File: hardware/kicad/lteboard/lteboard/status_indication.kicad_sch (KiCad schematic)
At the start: 17 parts, among them U2 PCA9535PW

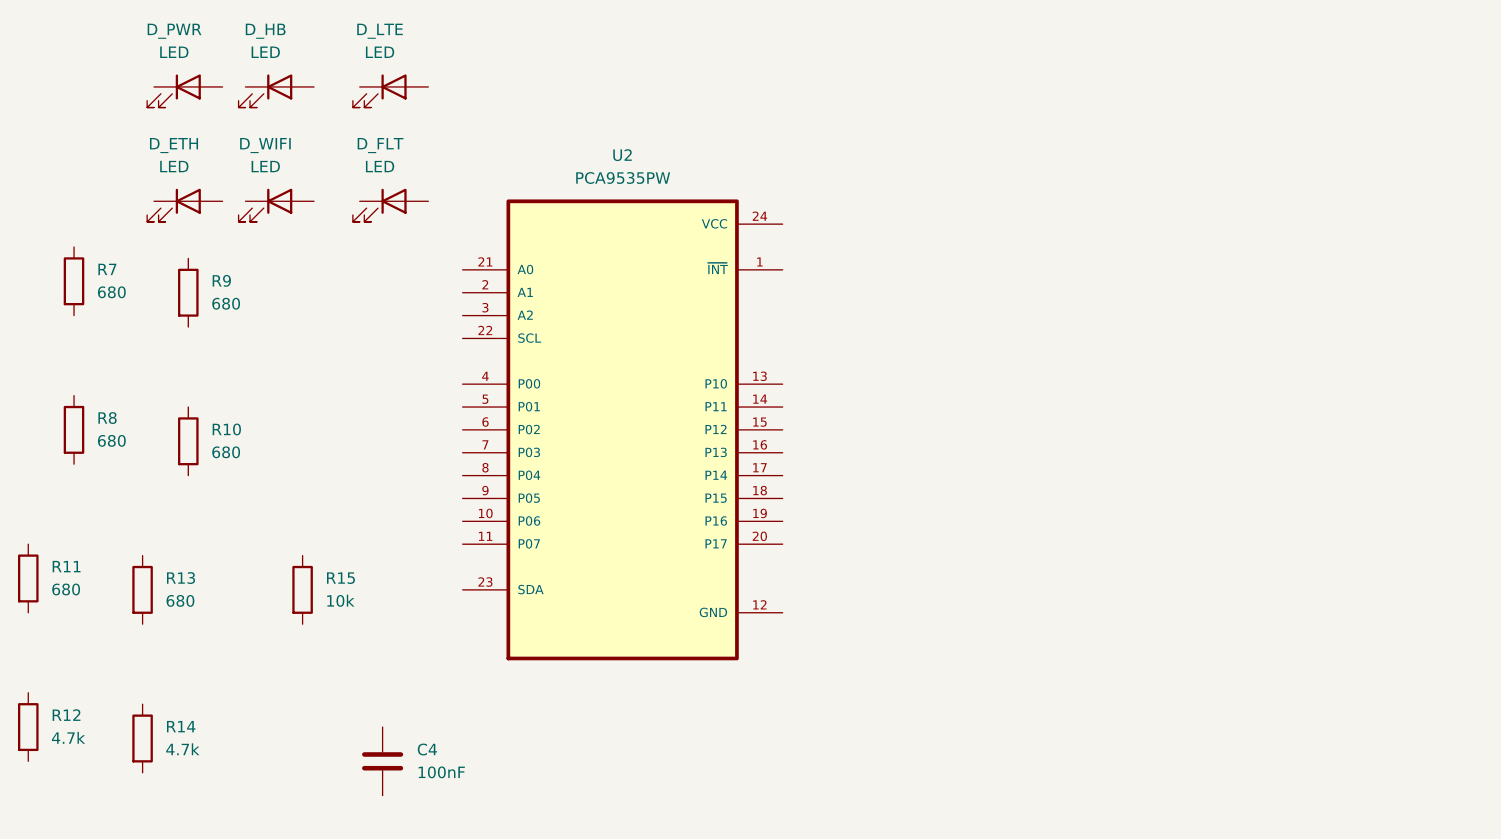
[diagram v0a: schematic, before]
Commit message: status-indication: complete schematic capture, cross-sheet wiring, docs, and BOM
- status_indication.kicad_sch: full wiring completed (address straps, power/ground,
  I2C pull-ups, INT pull-up, decoupling, 6 LED channels). Caught and fixed two real bugs
  via full programmatic connectivity verification (every pin/net reconstructed from the
  actual file, not just visual inspection): all 6 LEDs were initially wired with reversed
  polarity (would never have lit), and a new hierarchical 3V3_LOGIC label was placed
  floating (same name, no wire, so not actually part of the net). 10 spare GPIOs marked
  with No-Connect flags.
- core-compute.kicad_sch: converted 5 local GND_LOGIC labels to global_label (same class
  of bug fixed in power.kicad_sch during analog-io's ERC pass -- would have left this new
  sheet's ground isolated from the MCU's). Added I2C_SDA/I2C_SCL (Bidirectional, on
  GPIO8/GPIO9) and 3V3_LOGIC (Passive) hierarchical labels for cross-sheet export.
  Confirmed J1's 4 VBUS pins share one schematic pin location by symbol design, so the
  existing single No-Connect flag already covers all 4 -- no gap there.
- lteboard.kicad_sch: wired the two sheet symbols together (I2C_SDA, I2C_SCL, 3V3_LOGIC),
  verified pin types match on both ends (Passive/Passive, Bidirectional/Bidirectional x2)
  and wire endpoints land exactly on the corresponding pins.
- Added docs/subsystems/status-indication.md (full build-plan writeup, Steps 1-8) and
  hardware/bom/status_indication_bom.csv (10 parts).
- docs/roadmap.md: item 5 (status indication) marked DONE; backfilled item 4 (relay
  outputs) to DONE too, since it was already complete but never marked here.
- docs/build-log.md: added the status-indication entry, and backfilled the relay-outputs
  entry that was missing.

ERC deferred to a single project-wide pass once every subsystem is built, per current
project decision (not run per-subsystem here, unlike analog-io).

Deliberately not included: uncommitted analog-io changes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
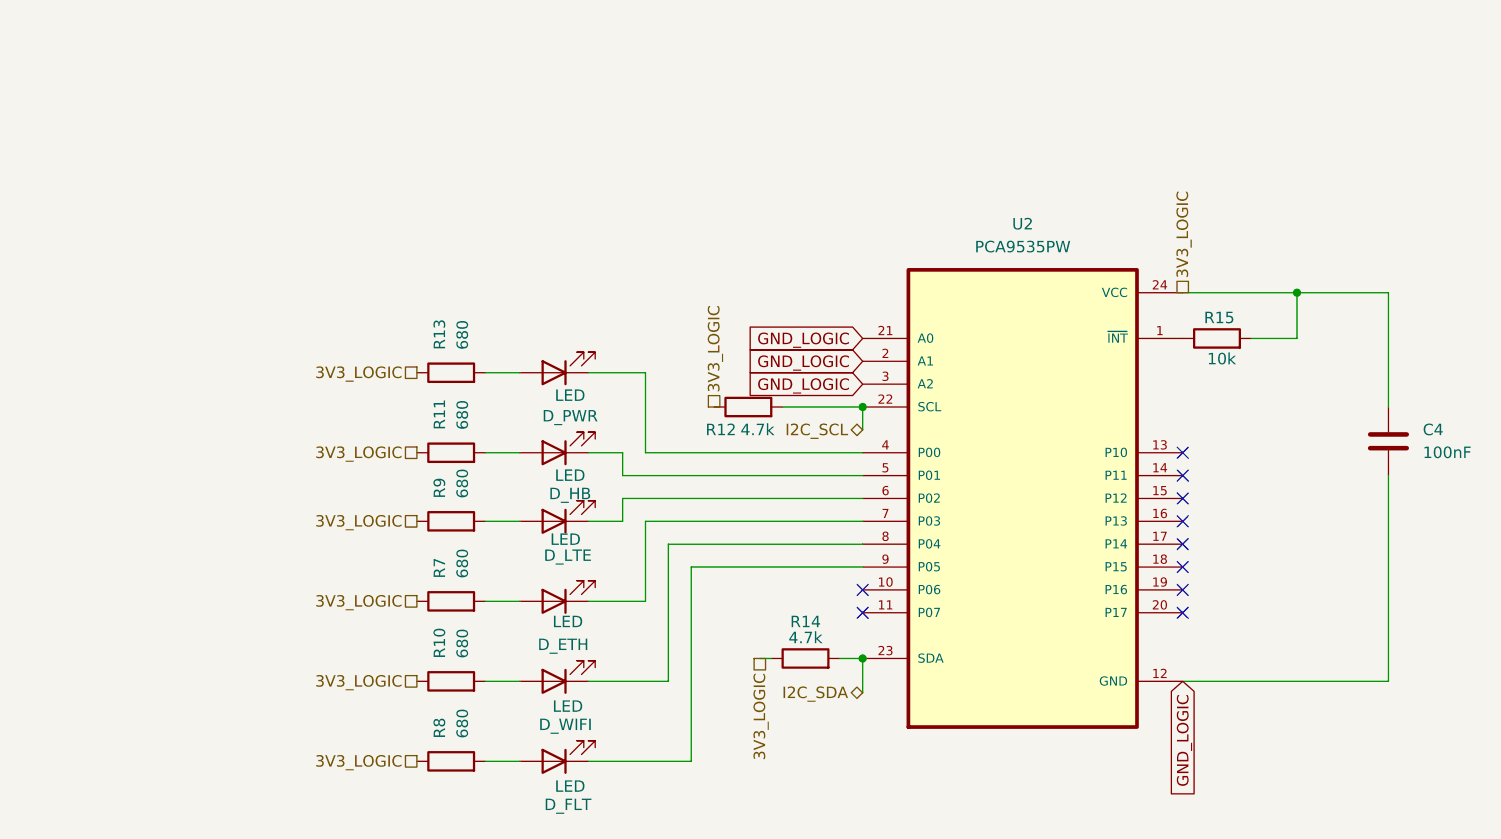
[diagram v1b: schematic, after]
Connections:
- net 3V3_LOGIC: now reaches R8.1
- net 3V3_LOGIC: now also C4.1, R10.1, R11.1, R12.1, R13.1, R14.1, R15.2, R7.1, R9.1, U2.24 (VCC)
- net at R8.2: now also D_FLT.2 (A)
- net at D_LTE.1 (K): now also U2.6 (P02)
- net at D_LTE.2 (A): now also R9.2
- net at D_ETH.1 (K): now also U2.7 (P03)
- net at D_ETH.2 (A): now also R7.2
- net at U2.1 (~{INT}): now also R15.1
- net GND_LOGIC: now reaches U2.12 (GND)
- net GND_LOGIC: now also C4.2, U2.2 (A1), U2.21 (A0), U2.3 (A2)
- net I2C_SCL: now reaches U2.22 (SCL)
- net I2C_SCL: now also R12.2
- net I2C_SDA: now reaches U2.23 (SDA)
- net I2C_SDA: now also R14.2
- net at U2.4 (P00): now also D_PWR.1 (K)
- net at U2.5 (P01): now also D_HB.1 (K)
- net at U2.8 (P04): now also D_WIFI.1 (K)
- net at U2.9 (P05): now also D_FLT.1 (K)
- net at D_PWR.2 (A): now also R13.2
- net at D_HB.2 (A): now also R11.2
- net at D_WIFI.2 (A): now also R10.2
- no-connect marks 0 -> 10
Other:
- moved on the sheet: C4, D_ETH, D_FLT, D_HB, D_LTE, D_PWR, D_WIFI, R10, R11, R12, R13, R14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
